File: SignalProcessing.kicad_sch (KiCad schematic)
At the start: 58 parts, among them J10 Header_50mil_1x05, J5 Header_100mil_1x06, J6 Header_100mil_1x06, J9 Header_50mil_1x05, U14 AD9833BRMZ-REEL7, U15 ADS131M04IPWR, U16 AD826

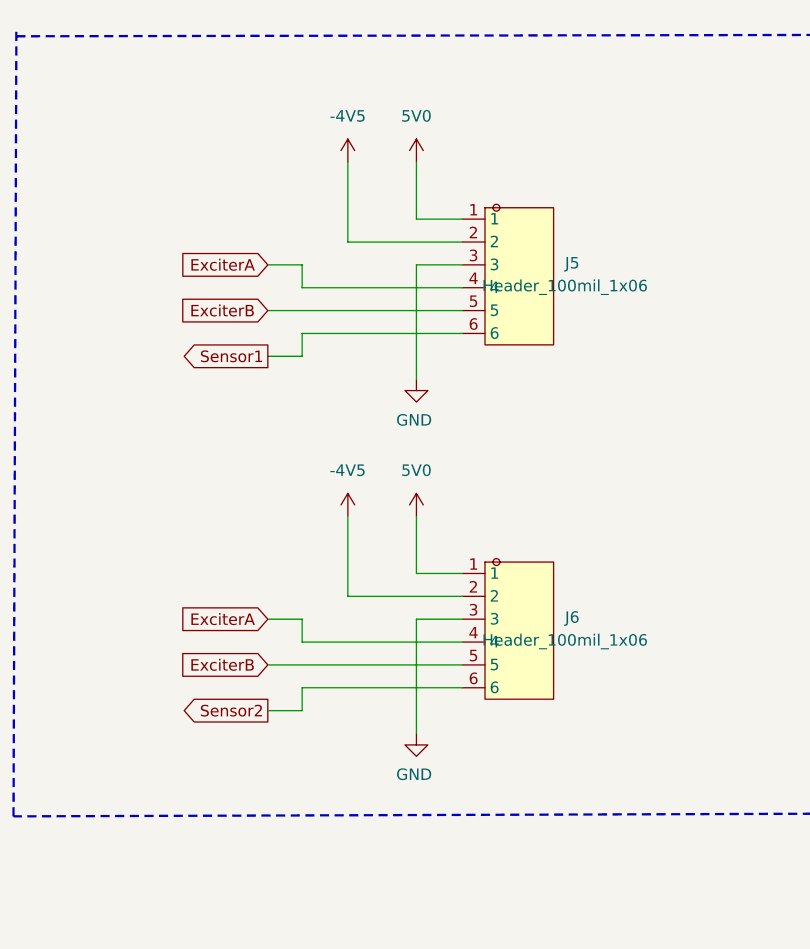
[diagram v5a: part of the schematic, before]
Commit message: Levelmeter sensor pinout changed. Font changed to bold
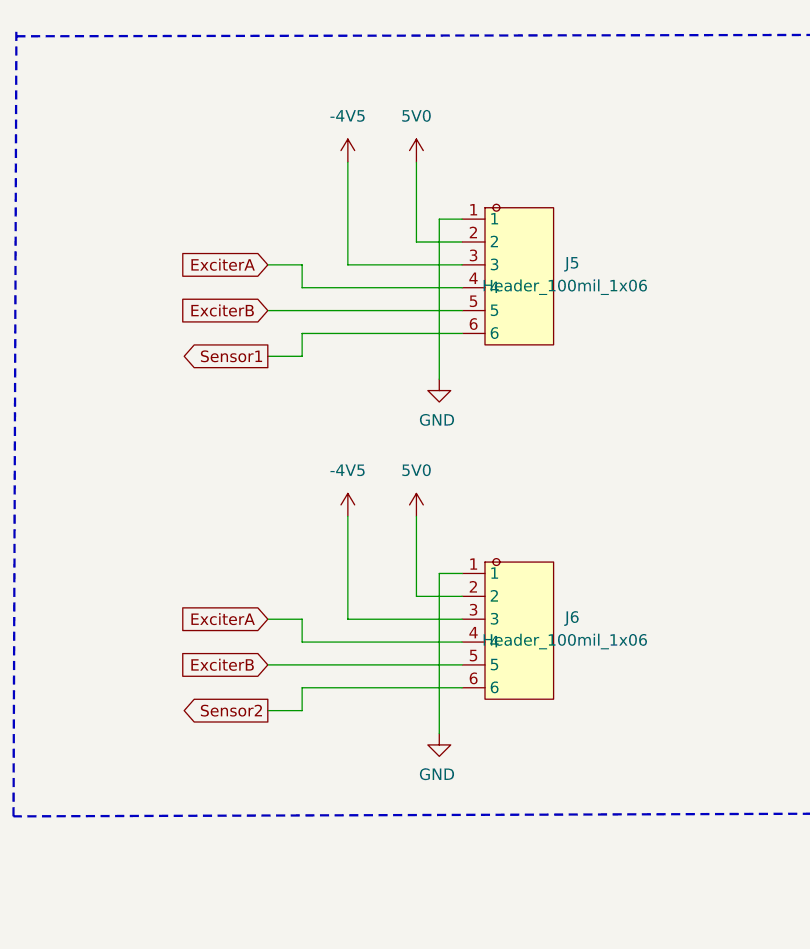
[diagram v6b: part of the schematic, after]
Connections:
- net -4V5: now also J5.3, J6.3; no longer J5.2, J6.2
- net 5V0: now also J5.2, J6.2; no longer J5.1, J6.1
- net GND: now also J5.1, J6.1; no longer J5.3, J6.3
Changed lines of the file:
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@@
 	(wire
 		(pts
-			(xy 344.17 184.15) (xy 344.17 175.26)
-		)
-		(stroke
-			(width 0)
-			(type default)
-		)
-	)
-	(wire
-		(pts
 			(xy 294.64 71.12) (xy 294.64 76.2)
 		)
@@
 	(wire
 		(pts
+			(xy 344.17 175.26) (xy 344.17 186.69)
+		)
+		(stroke
+			(width 0)
+			(type default)
+		)
+	)
+	(wire
+		(pts
 			(xy 77.47 203.2) (xy 77.47 204.47)
 		)
@@
 	(wire
 		(pts
-			(xy 344.17 223.52) (xy 344.17 214.63)
+			(xy 344.17 214.63) (xy 344.17 226.06)
 		)
 		(stroke
@@
 	(wire
 		(pts
-			(xy 351.79 220.98) (xy 351.79 214.63)
-		)
-		(stroke
-			(width 0)
-			(type default)
-		)
-	)
-	(wire
-		(pts
 			(xy 191.77 205.74) (xy 191.77 208.28)
 		)
@@
 	(wire
 		(pts
-			(xy 356.87 220.98) (xy 351.79 220.98)
-		)
-		(stroke
-			(width 0)
-			(type default)
-		)
-	)
-	(wire
-		(pts
 			(xy 232.41 210.82) (xy 264.16 210.82)
 		)
@@
 	(wire
 		(pts
+			(xy 356.87 226.06) (xy 344.17 226.06)
+		)
+		(stroke
+			(width 0)
+			(type default)
+		)
+	)
+	(wire
+		(pts
 			(xy 179.07 229.87) (xy 179.07 234.95)
 		)
@@
 	(wire
 		(pts
-			(xy 351.79 186.69) (xy 351.79 199.39)
+			(xy 354.33 181.61) (xy 354.33 199.39)
 		)
 		(stroke
@@
 	(wire
 		(pts
-			(xy 356.87 226.06) (xy 351.79 226.06)
-		)
-		(stroke
-			(width 0)
-			(type default)
-		)
-	)
-	(wire
-		(pts
 			(xy 276.86 102.87) (xy 276.86 104.14)
 		)
@@
 	(wire
 		(pts
+			(xy 356.87 223.52) (xy 351.79 223.52)
+		)
+		(stroke
+			(width 0)
+			(type default)
+		)
+	)
+	(wire
+		(pts
 			(xy 194.31 218.44) (xy 191.77 218.44)
 		)
@@
 	(wire
 		(pts
+			(xy 354.33 220.98) (xy 354.33 238.76)
+		)
+		(stroke
+			(width 0)
+			(type default)
+		)
+	)
+	(wire
+		(pts
 			(xy 120.65 91.44) (xy 120.65 92.71)
 		)
@@
 	(wire
 		(pts
-			(xy 351.79 181.61) (xy 351.79 175.26)
+			(xy 351.79 175.26) (xy 351.79 184.15)
 		)
 		(stroke
@@
 	(wire
 		(pts
-			(xy 356.87 184.15) (xy 344.17 184.15)
-		)
-		(stroke
-			(width 0)
-			(type default)
-		)
-	)
-	(wire
-		(pts
 			(xy 77.47 149.86) (xy 77.47 151.13)
 		)
@@
 	(wire
 		(pts
+			(xy 356.87 181.61) (xy 354.33 181.61)
+		)
+		(stroke
+			(width 0)
+			(type default)
+		)
+	)
+	(wire
+		(pts
+			(xy 356.87 186.69) (xy 344.17 186.69)
+		)
+		(stroke
+			(width 0)
+			(type default)
+		)
+	)
+	(wire
+		(pts
 			(xy 60.96 191.77) (xy 72.39 191.77)
 		)
@@
 	(wire
 		(pts
-			(xy 356.87 186.69) (xy 351.79 186.69)
+			(xy 351.79 214.63) (xy 351.79 223.52)
 		)
 		(stroke
@@
 	(wire
 		(pts
+			(xy 356.87 184.15) (xy 351.79 184.15)
+		)
+		(stroke
+			(width 0)
+			(type default)
+		)
+	)
+	(wire
+		(pts
 			(xy 120.65 86.36) (xy 120.65 85.09)
 		)
@@
 	(wire
 		(pts
+			(xy 356.87 220.98) (xy 354.33 220.98)
+		)
+		(stroke
+			(width 0)
+			(type default)
+		)
+	)
+	(wire
+		(pts
 			(xy 50.8 191.77) (xy 55.88 191.77)
 		)
@@
 	(wire
 		(pts
-			(xy 351.79 226.06) (xy 351.79 238.76)
-		)
-		(stroke
-			(width 0)
-			(type default)
-		)
-	)
-	(wire
-		(pts
 			(xy 290.83 66.04) (xy 290.83 83.82)
 		)
@@
 	(wire
 		(pts
-			(xy 356.87 181.61) (xy 351.79 181.61)
-		)
-		(stroke
-			(width 0)
-			(type default)
-		)
-	)
-	(wire
-		(pts
 			(xy 255.27 229.87) (xy 255.27 234.95)
 		)
@@
 	(wire
 		(pts
-			(xy 356.87 223.52) (xy 344.17 223.52)
-		)
-		(stroke
-			(width 0)
-			(type default)
-		)
-	)
-	(wire
-		(pts
 			(xy 194.31 208.28) (xy 191.77 208.28)
 		)
@@
 	(symbol
 		(lib_id "sldrnrd:PowerFlag/GND")
-		(at 351.79 238.76 0)
+		(at 354.33 238.76 0)
 		(unit 1)
 		(body_style 1)
@@
 		(dnp no)
 		(property "Reference" "#PWR0167"
-			(at 351.79 245.11 0)
+			(at 354.33 245.11 0)
 			(hide yes)
 			(show_name no)
@@
 		)
 		(property "Value" "GND"
-			(at 351.536 243.332 0)
+			(at 354.076 243.332 0)
 			(show_name no)
 			(do_not_autoplace no)
@@
 		)
 		(property "Footprint" ""
-			(at 351.79 238.76 0)
+			(at 354.33 238.76 0)
 			(hide yes)
 			(show_name no)
@@
 		)
 		(property "Datasheet" "~"
-			(at 351.79 238.76 0)
+			(at 354.33 238.76 0)
 			(hide yes)
 			(show_name no)
@@
 		)
 		(property "Description" "Power symbol creates a global label with name \"GND\", ground"
-			(at 351.79 238.76 0)
+			(at 354.33 238.76 0)
 			(hide yes)
 			(show_name no)
@@
 	(symbol
 		(lib_id "sldrnrd:PowerFlag/GND")
-		(at 351.79 199.39 0)
+		(at 354.33 199.39 0)
 		(unit 1)
 		(body_style 1)
@@
 		(dnp no)
 		(property "Reference" "#PWR0165"
-			(at 351.79 205.74 0)
+			(at 354.33 205.74 0)
 			(hide yes)
 			(show_name no)
@@
 		)
 		(property "Value" "GND"
-			(at 351.536 203.962 0)
+			(at 354.076 203.962 0)
 			(show_name no)
 			(do_not_autoplace no)
@@
 		)
 		(property "Footprint" ""
-			(at 351.79 199.39 0)
+			(at 354.33 199.39 0)
 			(hide yes)
 			(show_name no)
@@
 		)
 		(property "Datasheet" "~"
-			(at 351.79 199.39 0)
+			(at 354.33 199.39 0)
 			(hide yes)
 			(show_name no)
@@
 		)
 		(property "Description" "Power symbol creates a global label with name \"GND\", ground"
-			(at 351.79 199.39 0)
+			(at 354.33 199.39 0)
 			(hide yes)
 			(show_name no)

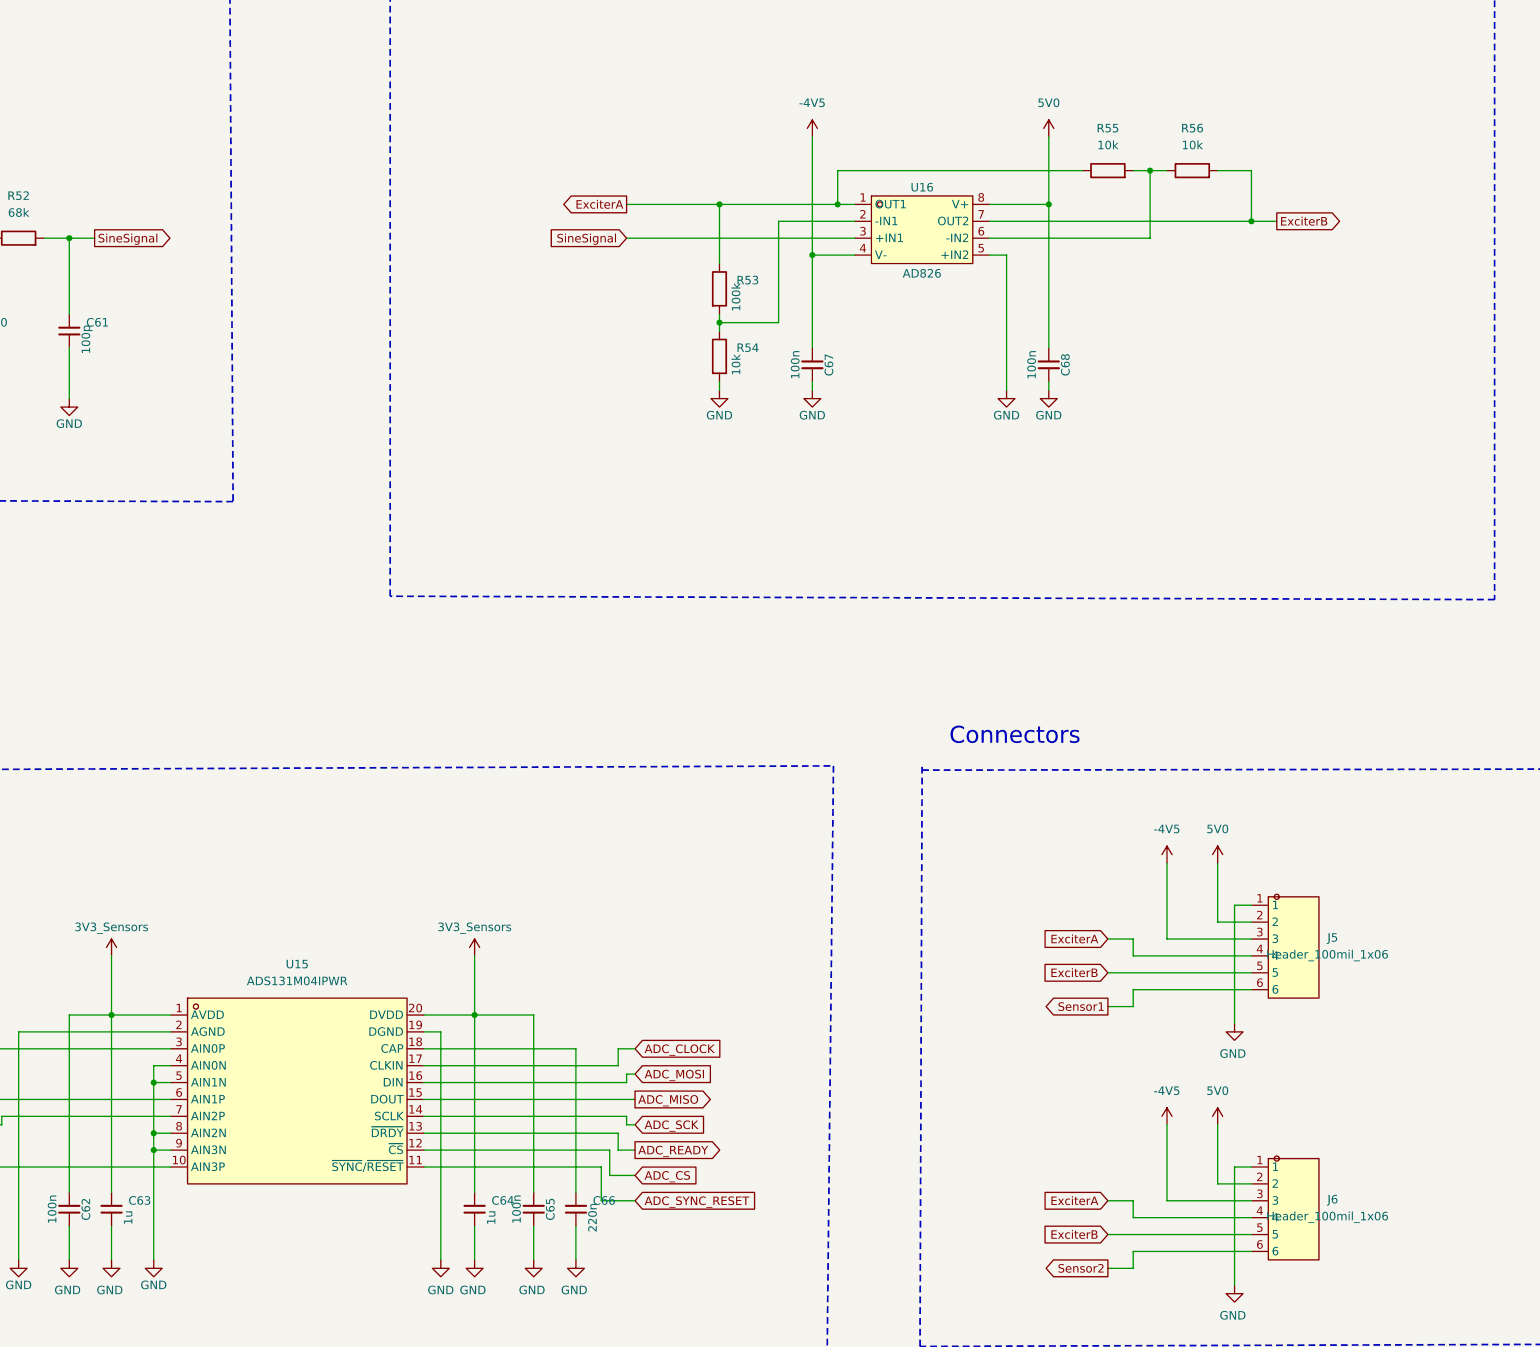
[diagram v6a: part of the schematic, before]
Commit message: Further checks. Capacitors unified to basic parts
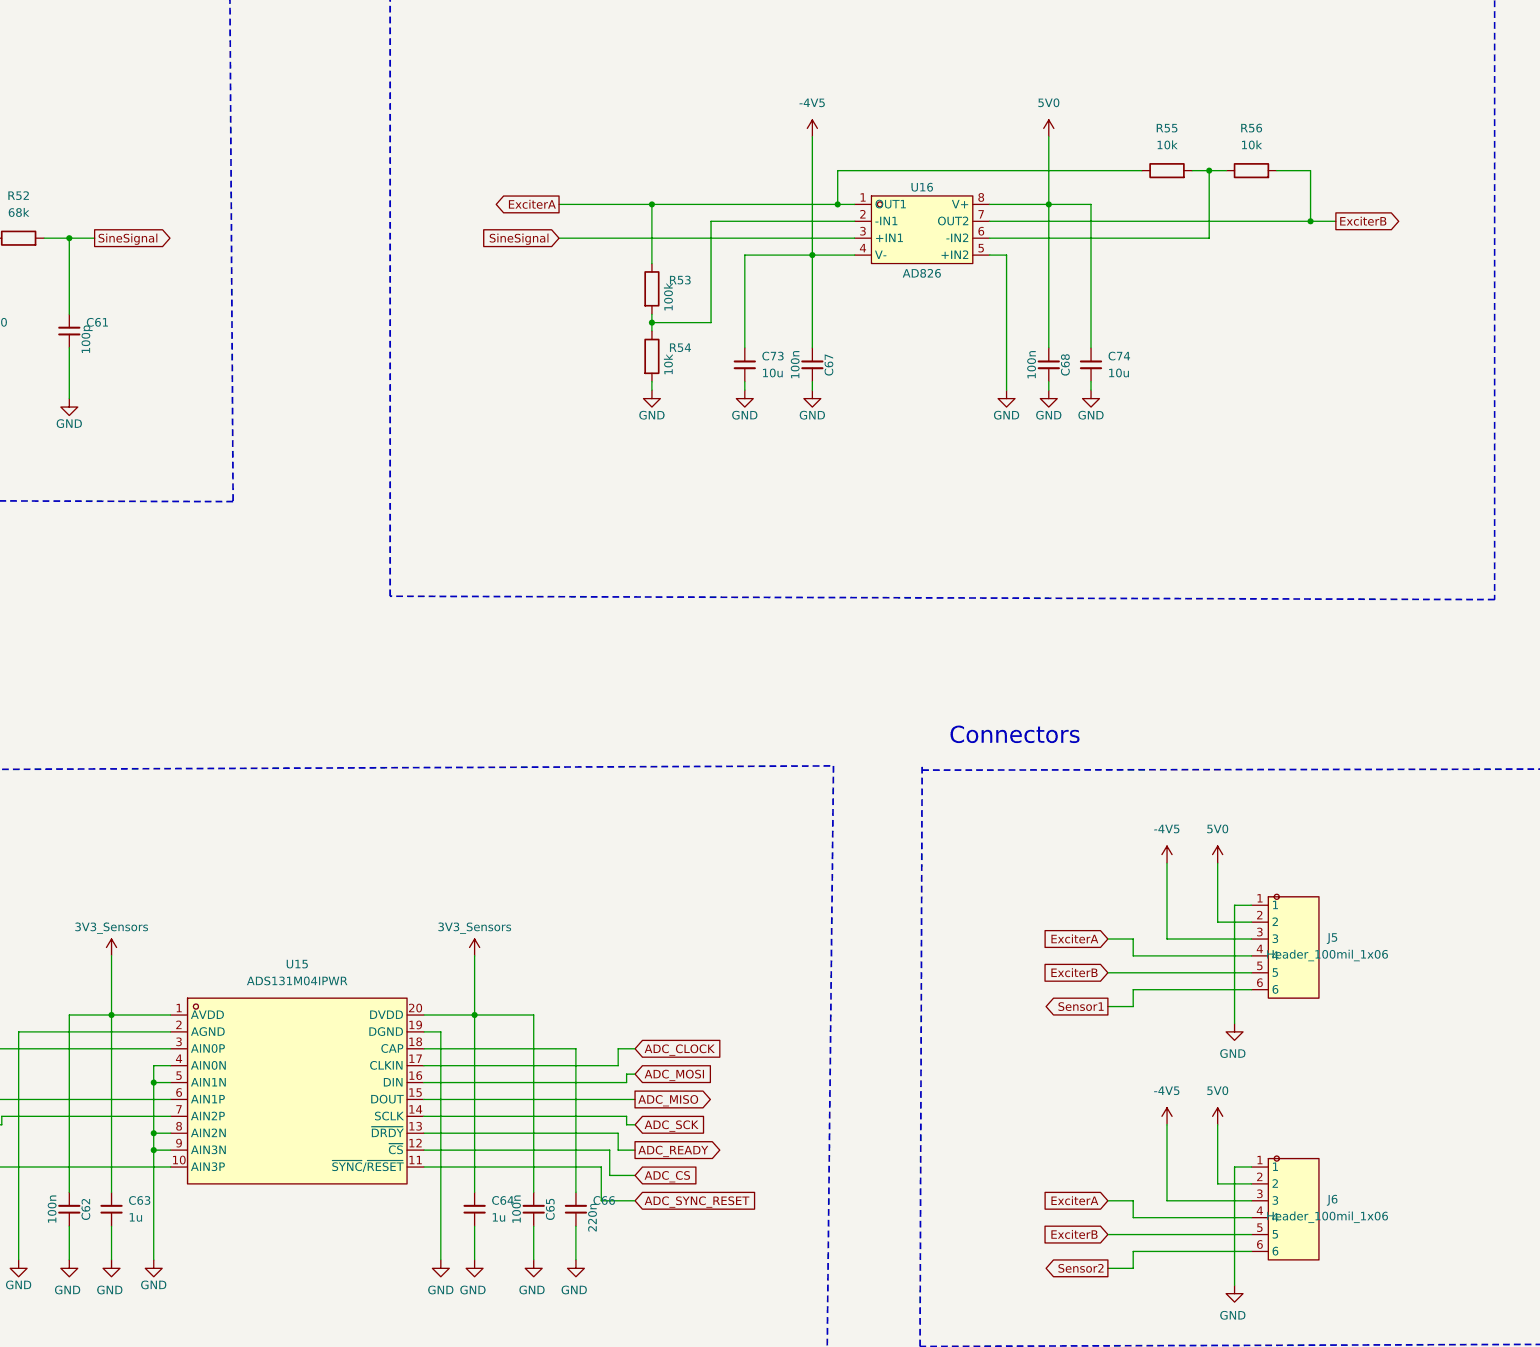
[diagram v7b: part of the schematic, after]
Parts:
- added C73, C74: 10u, sldrnrd:C_0805, symbol sldrnrd:Capacitor/C0805_10u
- C47: footprint sldrnrd:C_1206 -> sldrnrd:C_0805; symbol sldrnrd:Capacitor/C1206_10u -> sldrnrd:Capacitor/C0805_10u; Dielectric X7R -> X5R; LCSC C70462 -> C440198; MPN CC1206KKX7R8BB106 -> GRM21BR61H106KE43L; Manufacturer Yageo -> Murata; Voltage 25V -> 50V
- C63, C64: footprint sldrnrd:C_0603 -> sldrnrd:C_0805; symbol sldrnrd:Capacitor/C0603_1u -> sldrnrd:Capacitor/C0805_1u; LCSC C29936 -> C28323; MPN CL10B105KA8NNNC -> CL21B105KBFNNNE; Voltage 25V -> 50V
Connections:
- net -4V5: now also C73.1
- net 5V0: now also C74.1
- net GND: now also C73.2, C74.2
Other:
- moved on the sheet: R53, R54, R55, R56

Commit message: LEVELMETER Rev A as ordered
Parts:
- C55, C56, C57, C58: value 1n -> 10n; symbol sldrnrd:Capacitor/C0603_1n -> sldrnrd:Capacitor/C0603_10n; LCSC C1588 -> C57112; MPN CL10B102KB8NNNC -> 0603B103K500NT; Manufacturer Samsung -> Fenghua
- R42, R43, R44, R45: value 33k -> 10k; symbol sldrnrd:Resistor/R0603_33k -> sldrnrd:Resistor/R0603_10k; LCSC C4216 -> C25804; MPN 0603WAF3302T5E -> 0603WAF1002T5E
- R46, R47, R48, R49: value 6k8 -> 680k; symbol sldrnrd:Resistor/R0603_6k8 -> sldrnrd:Resistor/R0603_680k; LCSC C23212 -> C25822; MPN 0603WAF6801T5E -> 0603WAF6803T5E
